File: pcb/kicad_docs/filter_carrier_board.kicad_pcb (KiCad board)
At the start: 2 copper layers, 58.4 x 99.1 mm, 43 parts, among them J1 PJ301M-12, J10 power_in, J2 PJ301M-12, J3 PJ301M-12, J4 PJ301M-12, J5 PJ301M-12, J6 signal_in, J7 signal_out, J8 cv_in, J9 power_and_rez_cv_in, U1 TL072, U2 TL072, U3 MAX6035xxUR50

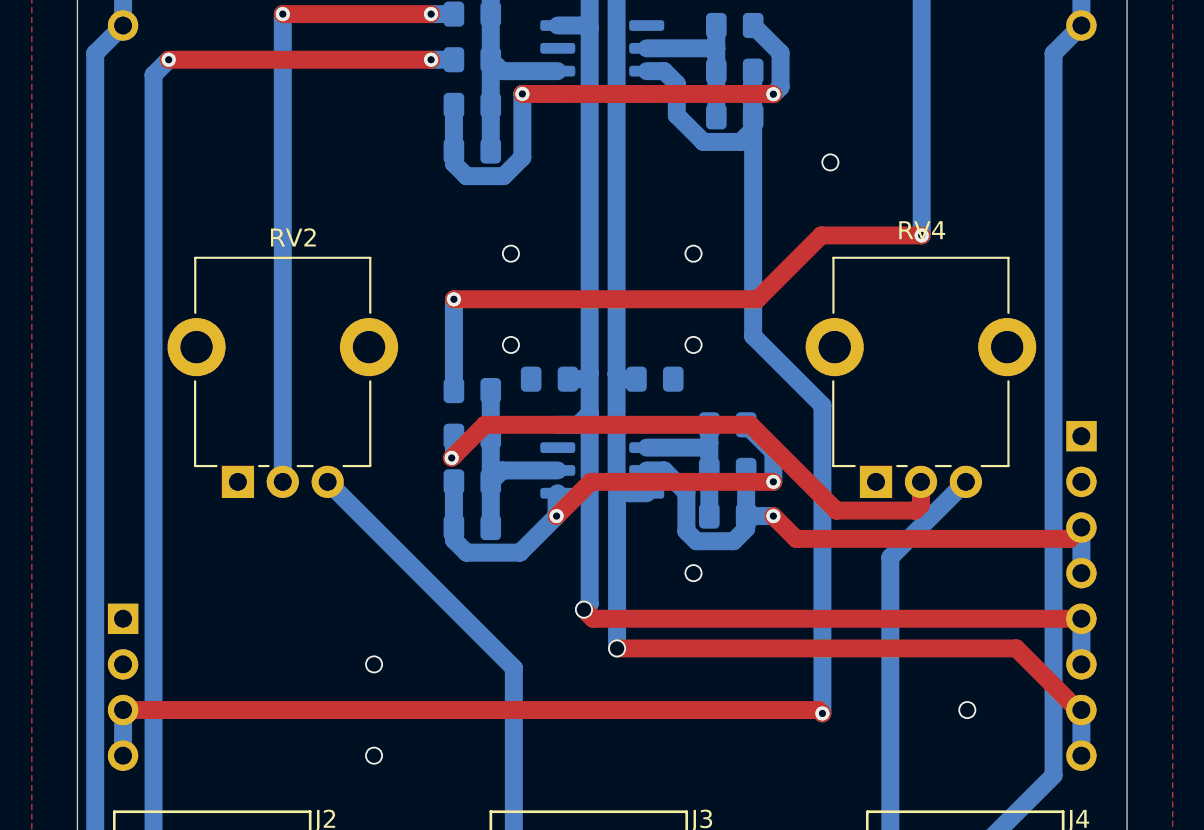
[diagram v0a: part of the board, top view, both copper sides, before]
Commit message: fix misplaced headers, update readme
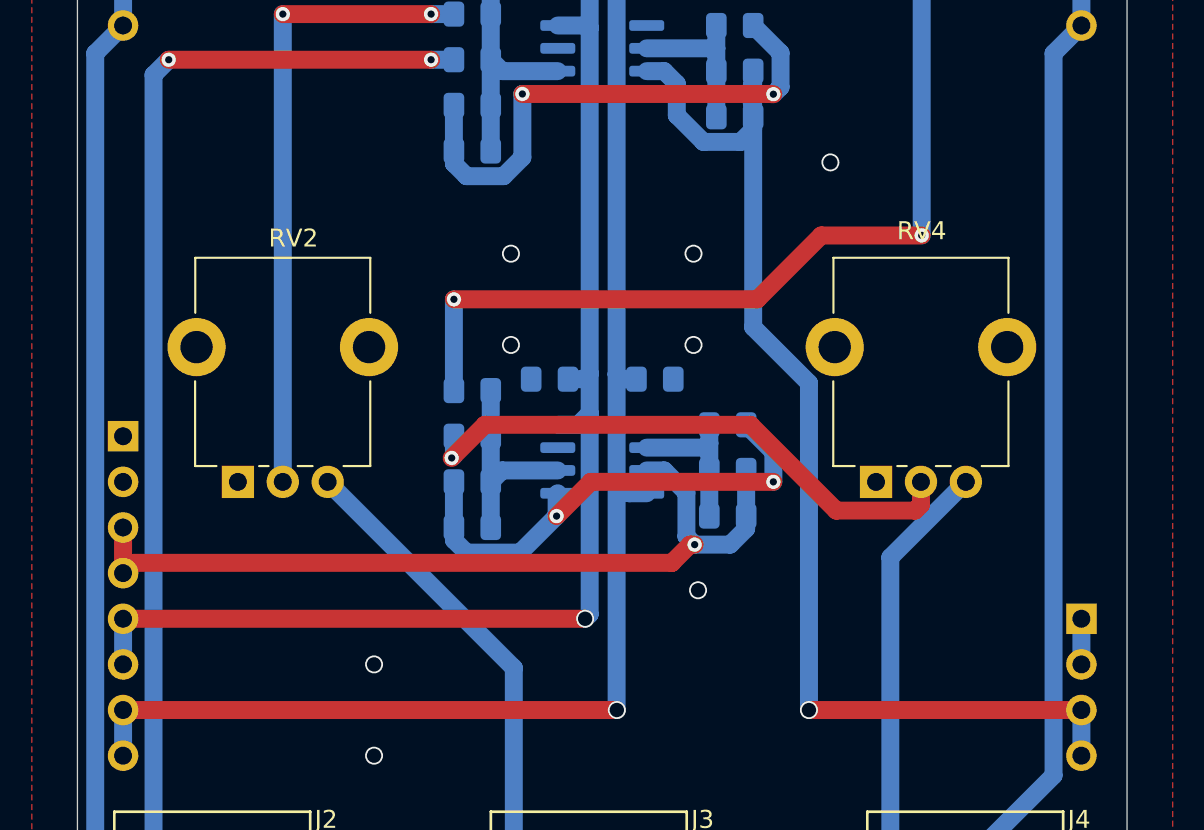
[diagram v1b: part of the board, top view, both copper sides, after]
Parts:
- moved J8 53.3 mm to (158.8, 111.8)
- moved J9 53.3 mm to (105.4, 101.6)
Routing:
- net Net-(C2-Pad1): track 88.5 -> 64.2 mm
- net Net-(C4-Pad1): track 33.9 -> 47.3 mm
- net +12V: track 122.9 -> 126.5 mm
- net GND: track 0.00 -> 2.54 mm, vias 11 -> 10
- net -12V: track 97.1 -> 95.4 mm

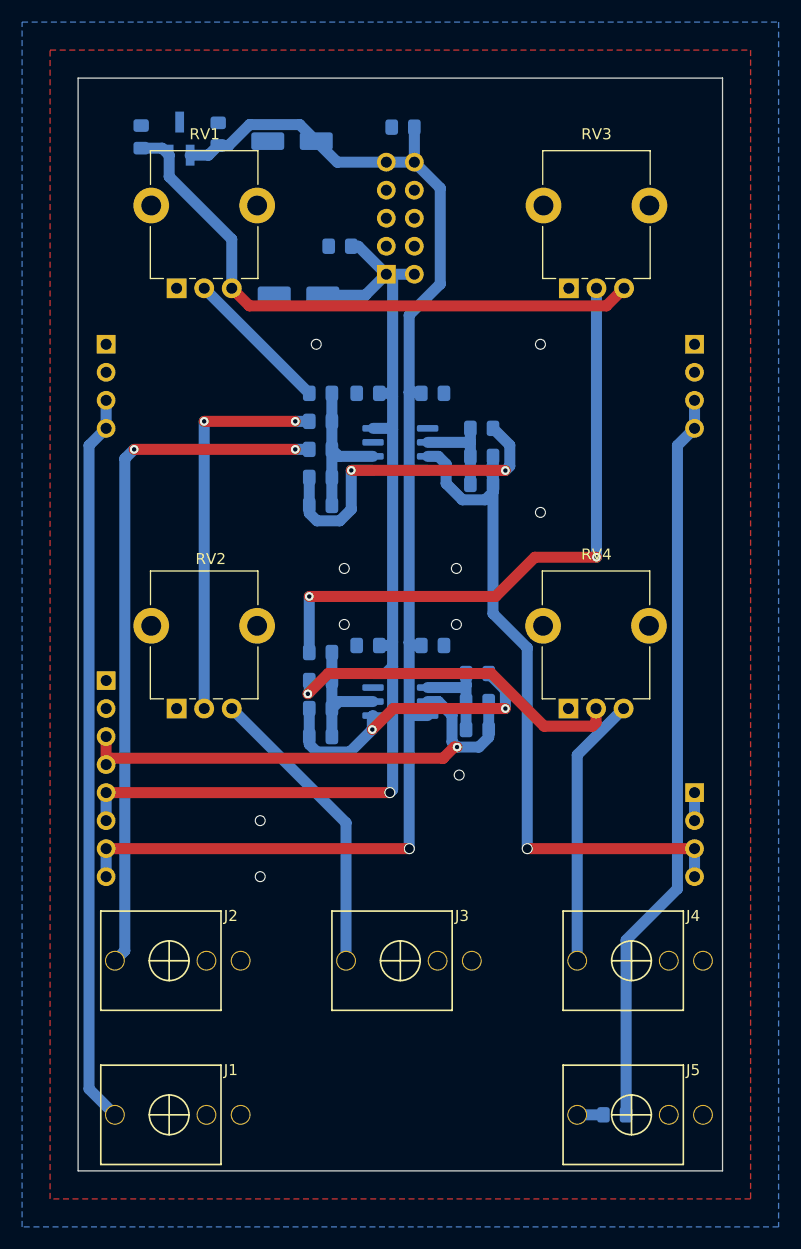
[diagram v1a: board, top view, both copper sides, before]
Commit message: fix header spacing issue
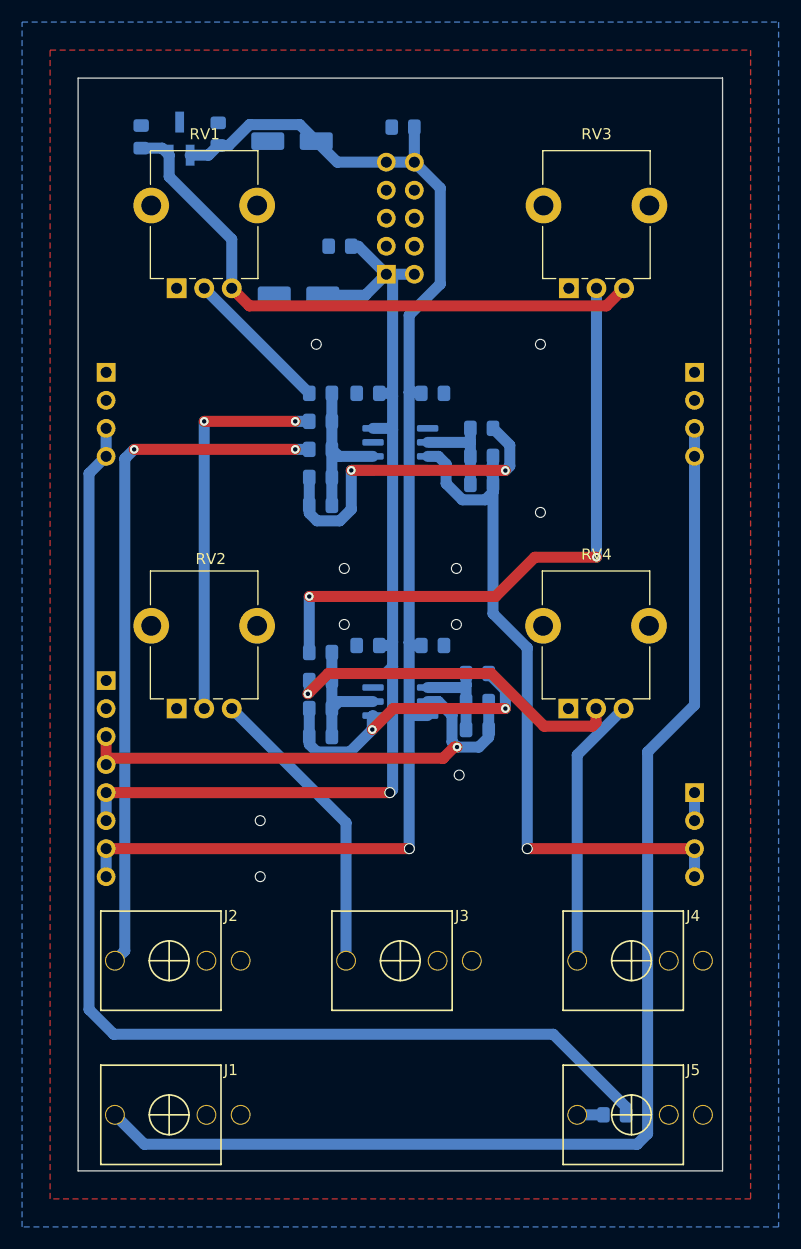
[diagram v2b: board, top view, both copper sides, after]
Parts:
- moved J6 53.4 mm to (158.8, 73.7)
- moved J7 53.4 mm to (105.4, 73.7)
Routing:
- net Net-(J1-Pad3): track 66.4 -> 115.5 mm
- net Net-(J7-Pad3): track 67.3 -> 106.4 mm
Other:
- board text added: "VCF plug-in board port"
- board text added: "github.com/JordanAceto/Filter_Carrier_Board rev 1.2 2020-08-19"
- board text removed: "github.com/JordanAceto/Filter_Carrier_Board rev 1.1 2020-07-13"
